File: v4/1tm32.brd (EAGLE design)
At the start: 50.8 x 50.8 mm, 44 parts, among them IC1 STM32L412RBT6P, J2 10118192-0001LF, SW1 LL3301FF065QJ, U2 LD39050PU33R, Y1 8MHz, Y2 32.7KHz

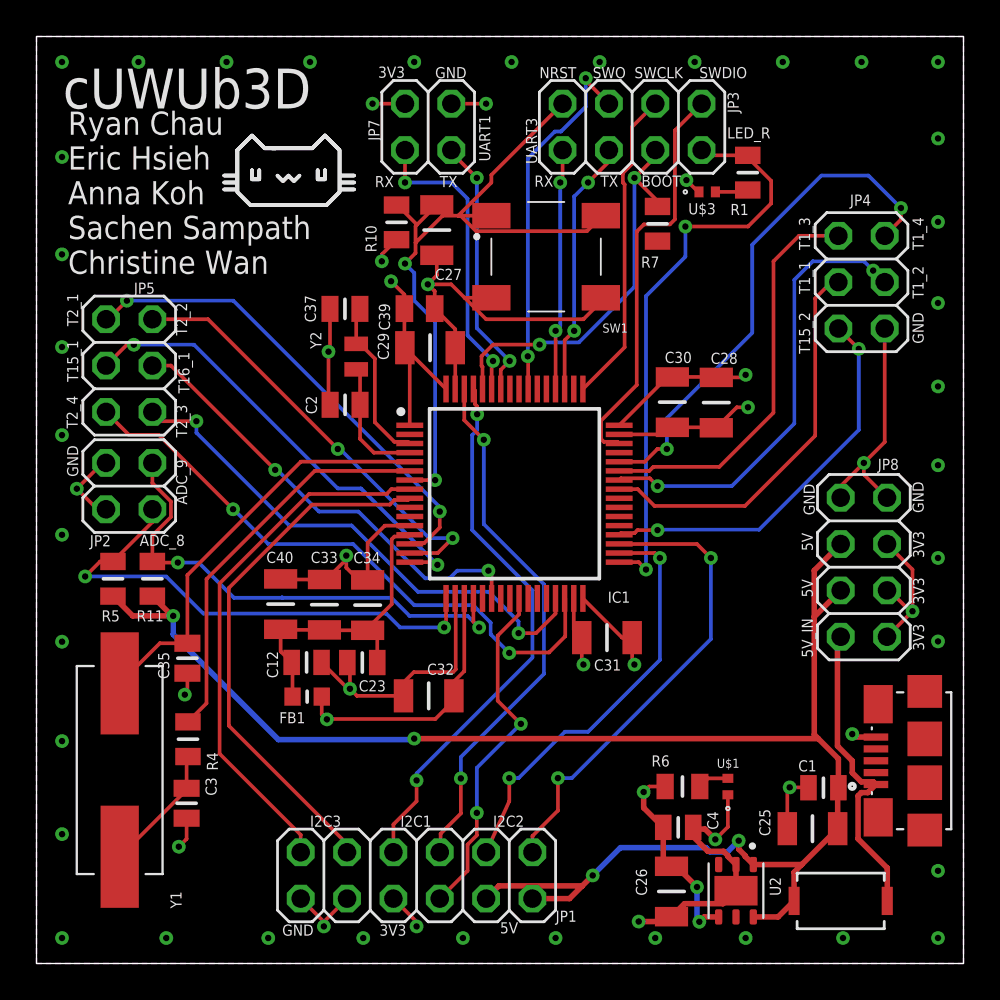
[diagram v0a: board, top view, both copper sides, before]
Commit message: moved wires around to meet design rules for JLC
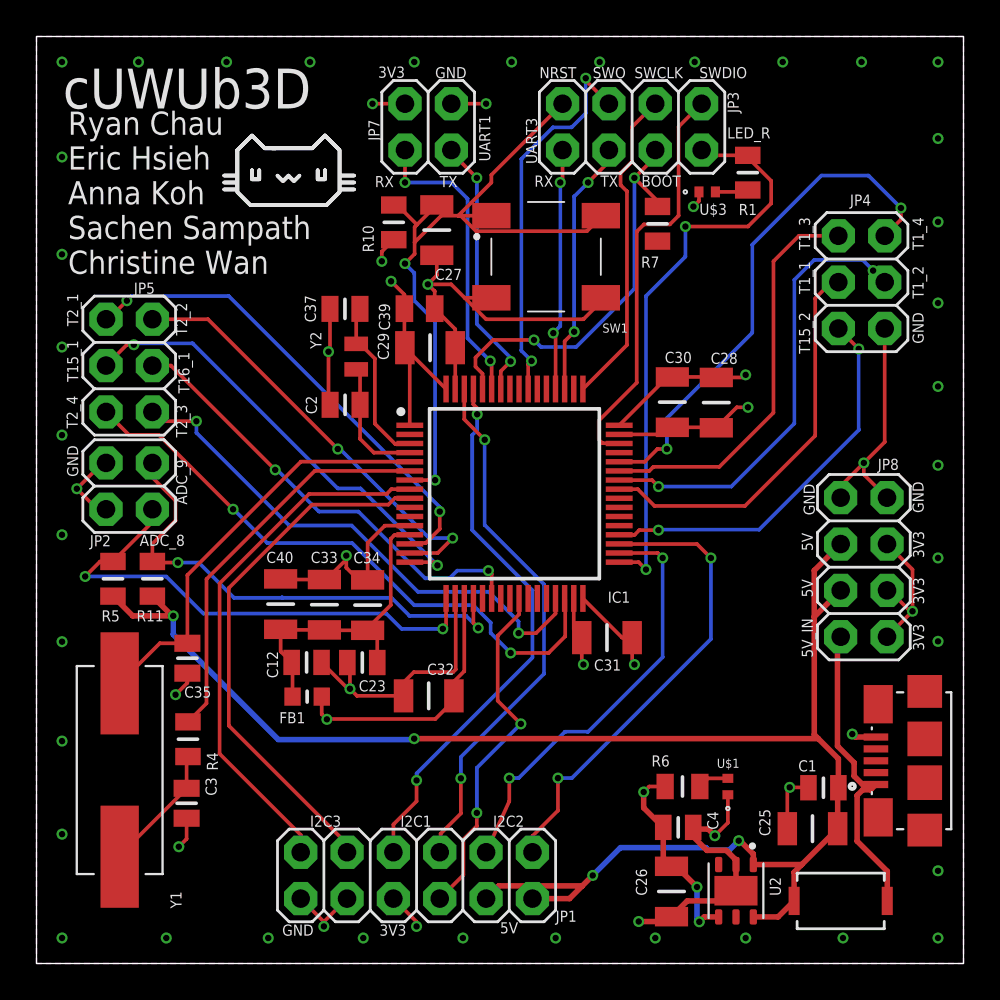
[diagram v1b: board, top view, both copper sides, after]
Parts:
- moved R10 0.15 mm to (19.6, 40.6)
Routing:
- net SWO: track 20.5 -> 21.3 mm
- net BOOT0: track 21.8 -> 22.6 mm
